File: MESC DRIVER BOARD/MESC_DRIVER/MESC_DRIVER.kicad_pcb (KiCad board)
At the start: 4 copper layers, 100 x 30 mm, 71 parts, among them J1 Conn_01x08_Male, J2 Conn_01x08_Male, J3 Conn_01x08_Male, J4 Conn_01x08_Male, J5 Conn_01x08_Male, J6 Conn_01x08_Male, J7 Conn_01x24_Male, U1 2EDL23N06, U2 INA240A2PW, U3 VIPer22AS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

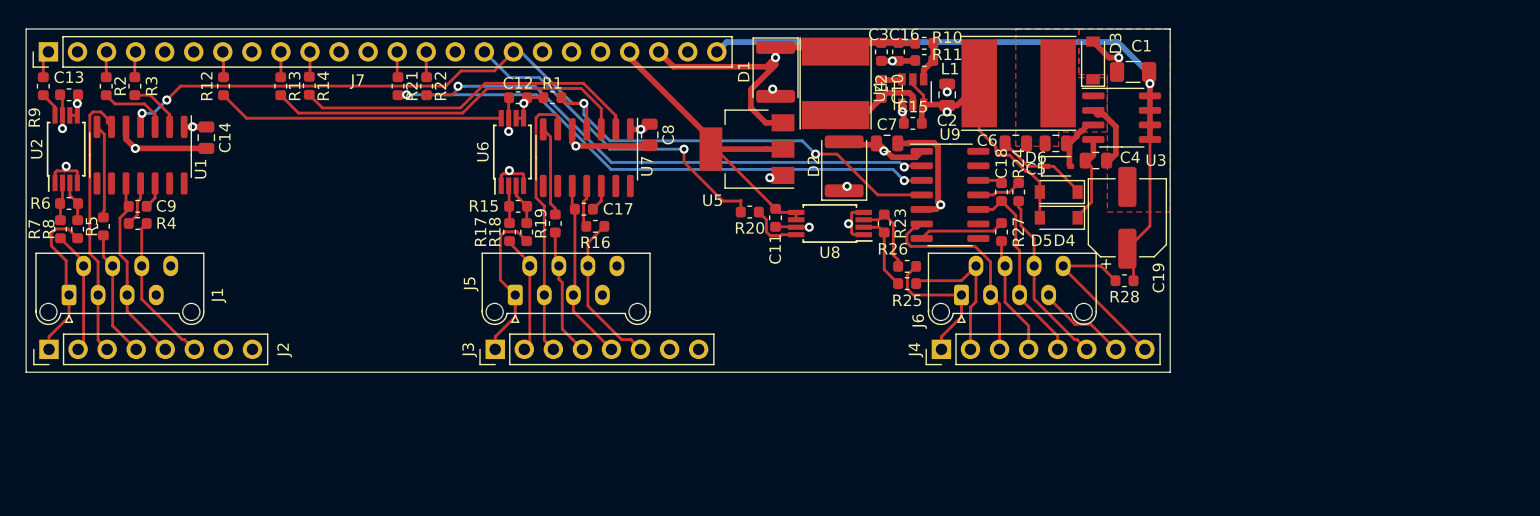
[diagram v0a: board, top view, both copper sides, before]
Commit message: Add DC bus voltage output to power board.
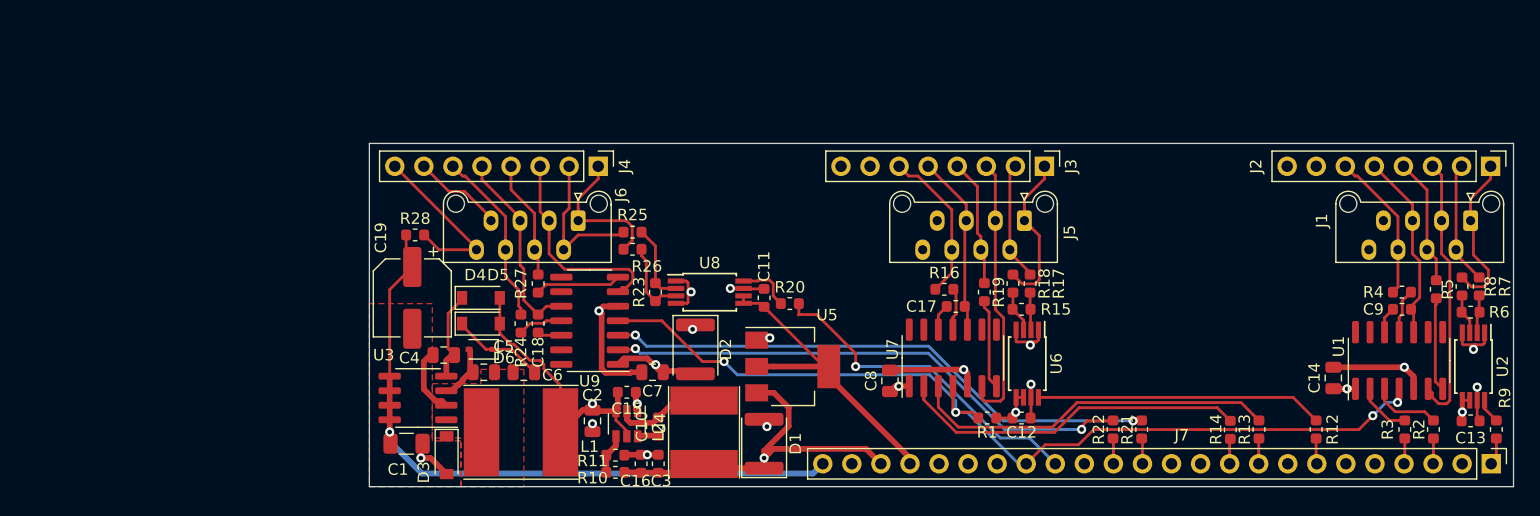
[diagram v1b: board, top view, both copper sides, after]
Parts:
- moved J7 131.1 mm to (178.1, 88.0), turned to 270 degrees
- moved R9 130.5 mm to (178.5, 85.0), turned to 270 degrees
- moved J2 127.0 mm to (178.0, 62.0), turned to 270 degrees
- moved C13 125.8 mm to (176.2, 84.2), turned to 0 degrees
- moved U2 124.5 mm to (176.5, 79.5), turned to 270 degrees
- moved R7 124.1 mm to (177.0, 72.5), turned to 90 degrees
- moved R6 122.9 mm to (176.2, 74.8), turned to 0 degrees
- moved J1 122.7 mm to (176.2, 66.8), turned to 270 degrees
- moved R8 121.1 mm to (175.5, 72.5), turned to 270 degrees
- moved R2 119.8 mm to (173.0, 85.0), turned to 90 degrees
- moved R5 116.6 mm to (173.2, 72.8), turned to 270 degrees
- moved R3 115.0 mm to (170.5, 85.0), turned to 270 degrees
- moved U1 111.5 mm to (170.0, 79.0), turned to 90 degrees
- moved C9 110.9 mm to (170.2, 74.5), turned to 0 degrees
- moved R4 110.7 mm to (170.2, 73.0), turned to 0 degrees
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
